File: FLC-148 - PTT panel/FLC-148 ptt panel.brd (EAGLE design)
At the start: 72 x 14.5 mm, 6 parts

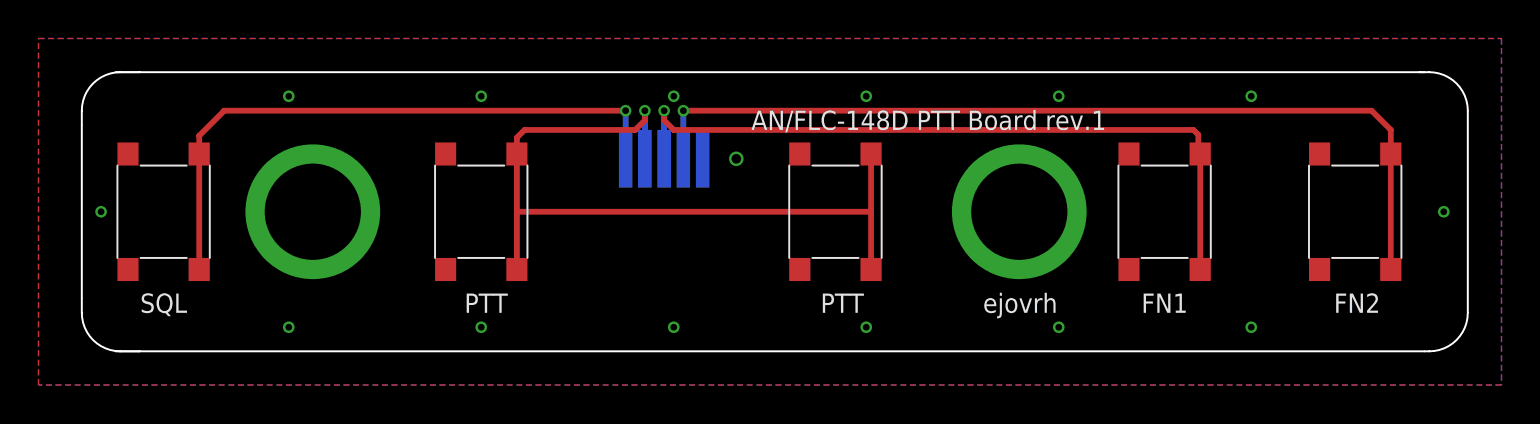
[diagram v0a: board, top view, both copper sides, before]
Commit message: start of rev.2 board: - replaced existing tact pushbuttons with lower profile ones
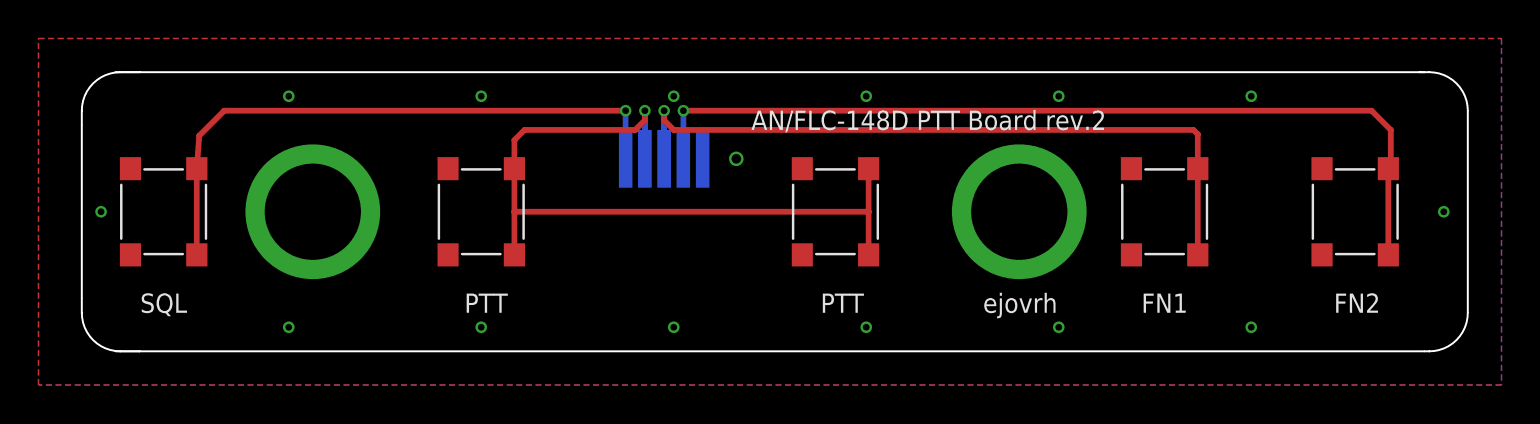
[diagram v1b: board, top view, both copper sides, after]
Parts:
- FN1, FN2, PTT_1, PTT_2, SQL: value 431151015826 -> TL3315NF250Q; device 431151015826 WS-TASV SMT Tact Pushbutton:SMD -> TL3315-345930 SMT Tact Pushbutton:SMT
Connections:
- net FN1: now also FN1.1; no longer FN1.4
- net FN2: now also FN2.1; no longer FN2.4
- net GND: now also FN1.4, FN2.4, PTT_1.4, PTT_2.4, SQL.4; no longer FN1.1, FN2.1, PTT_1.1, PTT_2.1, SQL.1
- net PTT: now also PTT_1.1, PTT_2.1; no longer PTT_1.4, PTT_2.4
- net SQL: now also SQL.1; no longer SQL.4
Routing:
- net PTT: track 41.3 -> 39.0 mm
- net FN1: track 38.1 -> 37.3 mm
- net SQL: track 32.1 -> 31.4 mm
- net FN2: track 46.9 -> 46.2 mm
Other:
- board text added: "AN/FLC-148D PTT Board rev.2"
- board text removed: "AN/FLC-148D PTT Board rev.1"

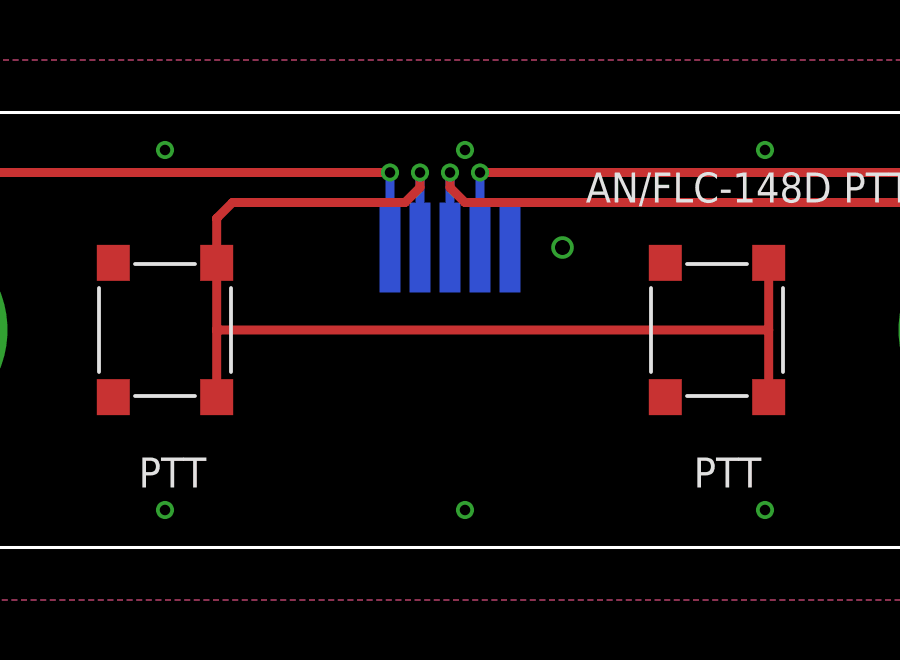
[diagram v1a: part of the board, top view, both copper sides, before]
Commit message: - moved FFC solder pad south to correct for cable orientation
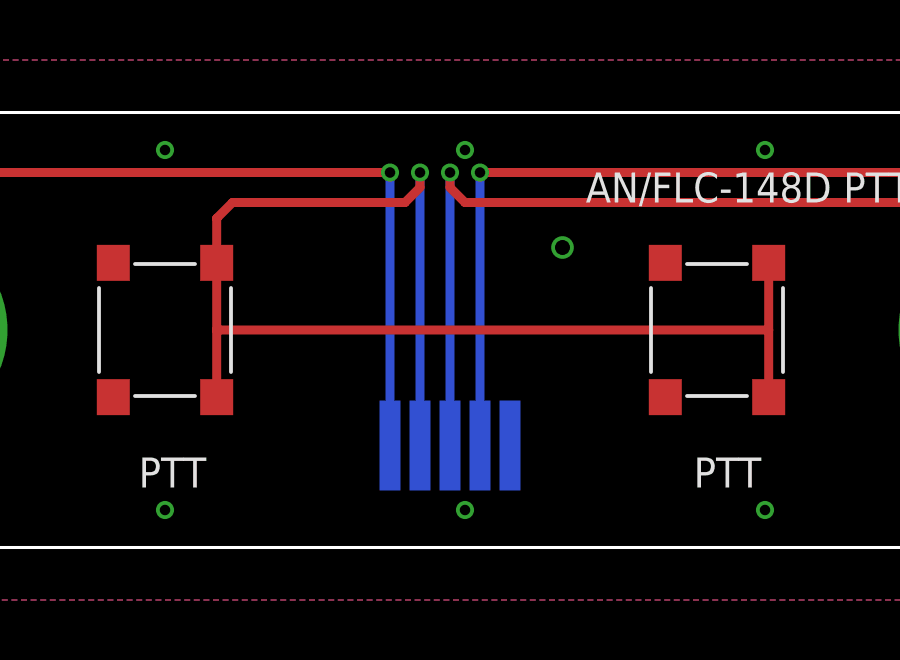
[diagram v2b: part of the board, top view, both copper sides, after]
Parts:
- moved MOTHERBOARD 6.60 mm to (30.2, -3.85)
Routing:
- net SQL: track 31.4 -> 38.0 mm
- net FN2: track 46.2 -> 52.8 mm
- net FN1: track 37.3 -> 43.9 mm
- net PTT: track 39.0 -> 45.6 mm
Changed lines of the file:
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@@
 <layer number="14" name="Route14" color="22" fill="1" visible="no" active="no"/>
 <layer number="15" name="Route15" color="23" fill="1" visible="no" active="no"/>
-<layer number="16" name="Bottom" color="1" fill="1" visible="yes" active="yes"/>
+<layer number="16" name="Bottom" color="1" fill="1" visible="no" active="yes"/>
 <layer number="17" name="Pads" color="2" fill="1" visible="yes" active="yes"/>
 <layer number="18" name="Vias" color="2" fill="1" visible="yes" active="yes"/>
@@
 <layer number="20" name="Dimension" color="24" fill="1" visible="yes" active="yes"/>
 <layer number="21" name="tPlace" color="7" fill="1" visible="yes" active="yes"/>
-<layer number="22" name="bPlace" color="7" fill="1" visible="yes" active="yes"/>
+<layer number="22" name="bPlace" color="7" fill="1" visible="no" active="yes"/>
 <layer number="23" name="tOrigins" color="15" fill="1" visible="yes" active="yes"/>
-<layer number="24" name="bOrigins" color="15" fill="1" visible="yes" active="yes"/>
-<layer number="25" name="tNames" color="7" fill="1" visible="no" active="yes"/>
+<layer number="24" name="bOrigins" color="15" fill="1" visible="no" active="yes"/>
+<layer number="25" name="tNames" color="7" fill="1" visible="yes" active="yes"/>
 <layer number="26" name="bNames" color="7" fill="1" visible="no" active="yes"/>
 <layer number="27" name="tValues" color="7" fill="1" visible="no" active="yes"/>
 <layer number="28" name="bValues" color="7" fill="1" visible="no" active="yes"/>
-<layer number="29" name="tStop" color="7" fill="3" visible="no" active="yes"/>
+<layer number="29" name="tStop" color="7" fill="3" visible="yes" active="yes"/>
 <layer number="30" name="bStop" color="7" fill="6" visible="no" active="yes"/>
 <layer number="31" name="tCream" color="7" fill="4" visible="no" active="yes"/>
@@
 <layer number="38" name="bTest" color="7" fill="1" visible="no" active="yes"/>
 <layer number="39" name="tKeepout" color="4" fill="11" visible="yes" active="yes"/>
-<layer number="40" name="bKeepout" color="1" fill="11" visible="yes" active="yes"/>
+<layer number="40" name="bKeepout" color="1" fill="11" visible="no" active="yes"/>
 <layer number="41" name="tRestrict" color="4" fill="10" visible="yes" active="yes"/>
-<layer number="42" name="bRestrict" color="1" fill="10" visible="yes" active="yes"/>
+<layer number="42" name="bRestrict" color="1" fill="10" visible="no" active="yes"/>
 <layer number="43" name="vRestrict" color="2" fill="10" visible="yes" active="yes"/>
 <layer number="44" name="Drills" color="7" fill="1" visible="no" active="yes"/>
@@
 <layer number="49" name="Reference" color="7" fill="1" visible="no" active="yes"/>
 <layer number="51" name="tDocu" color="7" fill="1" visible="yes" active="yes"/>
-<layer number="52" name="bDocu" color="7" fill="1" visible="yes" active="yes"/>
+<layer number="52" name="bDocu" color="7" fill="1" visible="no" active="yes"/>
 <layer number="88" name="SimResults" color="9" fill="1" visible="no" active="no"/>
 <layer number="89" name="SimProbes" color="9" fill="1" visible="no" active="no"/>
@@
 <wire x1="37.625" y1="6.25" x2="37.625" y2="-5.75" width="0.3" layer="22"/>
 <wire x1="37.625" y1="-5.75" x2="22.875" y2="-5.75" width="0.3" layer="22"/>
-<wire x1="22.875" y1="-5.75" x2="22.875" y2="0.75" width="0.3" layer="22"/>
-<text x="26.5" y="4" size="1" layer="26" font="vector" rot="MR90" align="center-right">GND</text>
-<text x="21.5" y="4" size="1" layer="26" font="vector" rot="MR90" align="center-right">SQL</text>
-<text x="22.75" y="4" size="1" layer="26" font="vector" rot="MR90" align="center-right">PTT</text>
-<text x="24" y="4" size="1" layer="26" font="vector" rot="MR90" align="center-right">FN1</text>
-<text x="25.25" y="4" size="1" layer="26" font="vector" rot="MR90" align="center-right">FN2</text>
+<wire x1="22.875" y1="-5.75" x2="22.875" y2="-5.05" width="0.3" layer="22"/>
+<text x="25.7" y="-2.4" size="1" layer="26" font="vector" rot="MR90" align="center-right">GND</text>
+<text x="20.7" y="-2.4" size="1" layer="26" font="vector" rot="MR90" align="center-right">SQL</text>
+<text x="21.95" y="-2.4" size="1" layer="26" font="vector" rot="MR90" align="center-right">PTT</text>
+<text x="23.2" y="-2.4" size="1" layer="26" font="vector" rot="MR90" align="center-right">FN1</text>
+<text x="24.45" y="-2.4" size="1" layer="26" font="vector" rot="MR90" align="center-right">FN2</text>
 <dimension x1="4.25" y1="0" x2="20.75" y2="0" x3="12.5" y3="-11.5" textsize="1.778" layer="47"/>
 <dimension x1="20.75" y1="0" x2="39.15" y2="0" x3="29.95" y3="-11.5" textsize="1.778" layer="47"/>
@@
 <text x="39.5" y="-4.75" size="1" layer="25" font="vector" rot="R180" align="center">PTT</text>
 <wire x1="37.625" y1="6.25" x2="22.875" y2="6.25" width="0.3" layer="22"/>
-<wire x1="22.875" y1="4.75" x2="22.875" y2="6.25" width="0.3" layer="22"/>
+<wire x1="22.875" y1="-1.75" x2="22.875" y2="6.25" width="0.3" layer="22"/>
 <wire x1="0" y1="4.5" x2="0" y2="5.25" width="0.1" layer="20"/>
 <wire x1="0" y1="5.25" x2="2" y2="7.25" width="0.1" layer="20" curve="-90"/>
@@
 <attribute name="VALUE" x="62.55" y="0" size="1" layer="27" font="vector" rot="R270" align="center"/>
 </element>
-<element name="MOTHERBOARD" library="FFC solder pad pitch 1mm 5p" package="FFC_1MM_5P" value="FFC 5p, 1mm pitch, solderpad" x="30.25" y="2.75" smashed="yes" rot="MR270">
-<attribute name="NAME" x="35.75" y="0.25" size="1" layer="26" font="vector" rot="MR90" align="center"/>
-<attribute name="VALUE" x="34.25" y="2.75" size="1" layer="28" font="vector" rot="MR270" align="center"/>
+<element name="MOTHERBOARD" library="FFC solder pad pitch 1mm 5p" package="FFC_1MM_5P" value="FFC 5p, 1mm pitch, solderpad" x="30.25" y="-3.85" smashed="yes" rot="MR270">
+<attribute name="NAME" x="35.75" y="-0.45" size="1" layer="26" font="vector" rot="MR90" align="center"/>
+<attribute name="VALUE" x="34.25" y="-3.85" size="1" layer="28" font="vector" rot="MR270" align="center"/>
 </element>
 </elements>
@@
 <wire x1="29.25" y1="5.25" x2="29.25" y2="4.75" width="0.3" layer="1"/>
 <contactref element="MOTHERBOARD" pad="P$4"/>
-<wire x1="29.25" y1="2.75" x2="29.25" y2="5.25" width="0.3" layer="16"/>
+<wire x1="29.25" y1="-3.85" x2="29.25" y2="5.25" width="0.3" layer="16"/>
 <wire x1="22.473" y1="2.238" x2="22.473" y2="3.723" width="0.3" layer="1"/>
 <wire x1="22.473" y1="3.723" x2="23" y2="4.25" width="0.3" layer="1"/>
@@
 <wire x1="30.25" y1="4.75" x2="30.75" y2="4.25" width="0.3" layer="1"/>
 <contactref element="MOTHERBOARD" pad="P$3"/>
-<wire x1="30.25" y1="2.75" x2="30.25" y2="5.25" width="0.3" layer="16"/>
+<wire x1="30.25" y1="-3.85" x2="30.25" y2="5.25" width="0.3" layer="16"/>
 <wire x1="57.973" y1="2.238" x2="57.973" y2="-2.238" width="0.3" layer="1"/>
 <wire x1="57.973" y1="2.238" x2="57.973" y2="4.027" width="0.3" layer="1"/>
@@
 <wire x1="7.4" y1="5.25" x2="6.1" y2="3.95" width="0.3" layer="1"/>
 <contactref element="MOTHERBOARD" pad="P$5"/>
-<wire x1="28.25" y1="2.75" x2="28.25" y2="5.25" width="0.3" layer="16"/>
+<wire x1="28.25" y1="-3.85" x2="28.25" y2="5.25" width="0.3" layer="16"/>
 <wire x1="5.973" y1="-2.238" x2="5.973" y2="2.238" width="0.3" layer="1"/>
 </signal>
@@
 <wire x1="68" y1="4.25" x2="67" y2="5.25" width="0.3" layer="1"/>
 <contactref element="MOTHERBOARD" pad="P$2"/>
-<wire x1="31.25" y1="2.75" x2="31.25" y2="5.25" width="0.3" layer="16"/>
+<wire x1="31.25" y1="-3.85" x2="31.25" y2="5.25" width="0.3" layer="16"/>
 <wire x1="67.873" y1="2.238" x2="67.873" y2="-2.238" width="0.3" layer="1"/>
 <wire x1="67.873" y1="2.238" x2="68" y2="2.365" width="0.3" layer="1"/>
